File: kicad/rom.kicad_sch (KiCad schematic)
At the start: 21 parts, among them U10 2764, U11 2764, U14 X2210, U15 74LS156, U16 7400, U17 74LS244, U18 74LS244, U19 74LS245, U6 2764, U62 74LS08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

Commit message: update kicad project
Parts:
- added U77: 74LS04, Package_DIP:DIP-14_W7.62mm, symbol 74xx:74LS04
- C5, C6: seq_coord (none) -> C4
- R5, RN4: seq_coord (none) -> C3
- R63, SP0: seq_coord (none) -> C10
- SP1: seq_coord (none) -> B1
- U10: footprint seequa_footprints:DIP-40_Socket_Compact -> Package_DIP:DIP-28_W15.24mm; seq_coord (none) -> B7; seq_silkscreen (none) -> E
- U11: footprint seequa_footprints:DIP-40_Socket_Compact -> Package_DIP:DIP-28_W15.24mm; seq_coord (none) -> B8; seq_silkscreen (none) -> F
- U14: seq_coord (none) -> C1
- U15: seq_coord (none) -> C2
- U16: seq_coord (none) -> C3; seq_silkscreen (none) -> 00
- U17: seq_coord (none) -> C5
- U18: seq_coord (none) -> C6; seq_notes ROM Address Buffer 8-10 -> ROM Address Buffer 8-13
- U19: seq_coord (none) -> C7; seq_notes ROM Data Bus Transceiver -> RAM/ROM Data Bus Transceiver; seq_silkscreen (none) -> LS245
- U6: footprint seequa_footprints:DIP-40_Socket_Compact -> Package_DIP:DIP-28_W15.24mm; seq_coord (none) -> B1
- U62: seq_coord (none) -> B10; seq_silkscreen (none) -> LS08
- U7: footprint seequa_footprints:DIP-40_Socket_Compact -> Package_DIP:DIP-28_W15.24mm; seq_coord (none) -> B3
- U74: seq_coord (none) -> D11
- U8: footprint seequa_footprints:DIP-40_Socket_Compact -> Package_DIP:DIP-28_W15.24mm; seq_coord (none) -> B4; seq_silkscreen (none) -> C
- U9: footprint seequa_footprints:DIP-40_Socket_Compact -> Package_DIP:DIP-28_W15.24mm; seq_coord (none) -> B6; seq_silkscreen (none) -> D
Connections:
- net GND: now also C6.2; no longer C6.1
- net ~{MEMR}: now also U77.11
- net ~{ROM_{CE}}: now reaches U7.20 (~{CE}), U74.14 (I/~{O_{3}})
- net at RN4.6 (R5.2), U15.6 (Q1a), U16.9: now also C6.1; no longer C6.2
- net ~{ARRAY_RECALL}: now reaches U14.10 (~{ARRAY_RECALL}), U16.11
- net DATA_DIR: now reaches U19.1 (A->B)
- net MRDC renamed MEMR
- net MEMR: now also U77.10
- net NVR_NAND_EXT renamed ~{RESET_{BRD}}
- net PALETTE0_SEL renamed ~{PALETTE0_{WR}}
- net PALETTE1_SEL renamed ~{PALETTE1_{WR}}
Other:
- note added: "To RAM (Page 3)"
- moved on the sheet: C6, U10, U11, U18, U6, U9

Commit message: More updates
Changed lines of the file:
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@@
+		)
+	)
+	(label "D[0..7]"
+		(at 337.82 139.7 270)
+		(effects
+			(font
+				(size 1.27 1.27)
+			)
+			(justify right bottom)
 		)
 	)

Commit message: Updates, chameleon logo
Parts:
- RN4: value 4.7K -> 4.7KΩ
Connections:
- net ~{ROM_{CE}} is gone; now on net BANK_EN_{B}: U7.20 (~{CE}), U74.14 (I/~{O_{3}})
- net BANK_EN_{B}: no longer U74.15 (I/~{O_{4}}), U8.20 (~{CE})
- net BANK_EN_{C}: now also U74.15 (I/~{O_{4}}), U8.20 (~{CE}); no longer U74.16 (I/~{O_{5}}), U9.20 (~{CE})
- net BANK_EN_{D}: now also U74.16 (I/~{O_{5}}), U9.20 (~{CE}); no longer U10.20 (~{CE}), U74.17 (I/~{O_{6}})
- net BANK_EN_{E}: now also U10.20 (~{CE}), U74.17 (I/~{O_{6}}); no longer U11.20 (~{CE}), U74.18 (I/~{O_{7}})
- new net BANK_EN_{F}: U11.20 (~{CE}), U74.18 (I/~{O_{7}})
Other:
- moved on the sheet: U62E

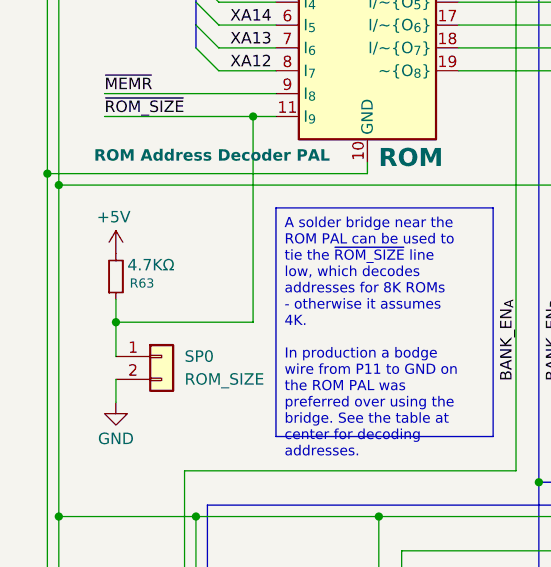
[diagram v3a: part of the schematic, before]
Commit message: A little work on composite output and GPIB
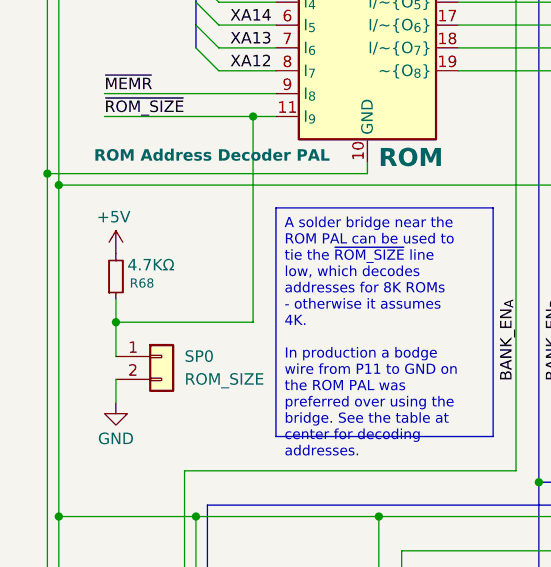
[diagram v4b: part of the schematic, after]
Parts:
- renumbered R63 to R68
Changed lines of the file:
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@@
 			(table_cell "~{ROM_SIZE}"
 				(exclude_from_sim no)
-				(at 240.03 226.06 0)
+				(at 158.75 226.06 0)
 				(size 15.24 2.54)
 				(margins 0.9525 0.9525 0.9525 0.9525)
@@
 			(table_cell ""
 				(exclude_from_sim no)
-				(at 247.65 226.06 0)
+				(at 166.37 226.06 0)
 				(size 7.62 2.54)
 				(margins 0.9525 0.9525 0.9525 0.9525)
@@
 			(table_cell "0 (8K)"
 				(exclude_from_sim no)
-				(at 240.03 228.6 0)
+				(at 158.75 228.6 0)
 				(size 7.62 2.54)
 				(margins 0.9525 0.9525 0.9525 0.9525)
@@
 			(table_cell "1 (4K)"
 				(exclude_from_sim no)
-				(at 247.65 228.6 0)
+				(at 166.37 228.6 0)
 				(size 7.62 2.54)
 				(margins 0.9525 0.9525 0.9525 0.9525)
@@
 				)
 			)
-			(table_cell "FE000"
+			(table_cell "FA000"
 				(exclude_from_sim no)
-				(at 240.03 231.14 0)
+				(at 158.75 231.14 0)
 				(size 7.62 2.54)
 				(margins 0.9525 0.9525 0.9525 0.9525)
@@
 				)
 			)
-			(table_cell "FF000"
+			(table_cell "FD000"
 				(exclude_from_sim no)
-				(at 247.65 231.14 0)
+				(at 166.37 231.14 0)
 				(size 7.62 2.54)
 				(margins 0.9525 0.9525 0.9525 0.9525)
@@
 			(table_cell "~{ROM_SIZE}"
 				(exclude_from_sim no)
-				(at 35.56 226.06 0)
+				(at 240.03 226.06 0)
 				(size 15.24 2.54)
 				(margins 0.9525 0.9525 0.9525 0.9525)
@@
 			(table_cell ""
 				(exclude_from_sim no)
-				(at 43.18 226.06 0)
+				(at 247.65 226.06 0)
 				(size 7.62 2.54)
 				(margins 0.9525 0.9525 0.9525 0.9525)
@@
 			(table_cell "0 (8K)"
 				(exclude_from_sim no)
-				(at 35.56 228.6 0)
+				(at 240.03 228.6 0)
 				(size 7.62 2.54)
 				(margins 0.9525 0.9525 0.9525 0.9525)
@@
 			(table_cell "1 (4K)"
 				(exclude_from_sim no)
-				(at 43.18 228.6 0)
+				(at 247.65 228.6 0)
 				(size 7.62 2.54)
 				(margins 0.9525 0.9525 0.9525 0.9525)
@@
 				)
 			)
-			(table_cell "F4000"
+			(table_cell "FE000"
 				(exclude_from_sim no)
-				(at 35.56 231.14 0)
+				(at 240.03 231.14 0)
 				(size 7.62 2.54)
 				(margins 0.9525 0.9525 0.9525 0.9525)
@@
 				)
 			)
-			(table_cell "FA000"
+			(table_cell "FF000"
 				(exclude_from_sim no)
-				(at 43.18 231.14 0)
+				(at 247.65 231.14 0)
 				(size 7.62 2.54)
 				(margins 0.9525 0.9525 0.9525 0.9525)
@@
 				(effects
 					(font
+						(face "Arial")
 						(size 1.27 1.27)
 					)
@@
 			(table_cell "~{ROM_SIZE}"
 				(exclude_from_sim no)
-				(at 158.75 226.06 0)
+				(at 77.47 226.06 0)
 				(size 15.24 2.54)
 				(margins 0.9525 0.9525 0.9525 0.9525)
@@
 			(table_cell ""
 				(exclude_from_sim no)
-				(at 166.37 226.06 0)
+				(at 85.09 226.06 0)
 				(size 7.62 2.54)
 				(margins 0.9525 0.9525 0.9525 0.9525)
@@
 			(table_cell "0 (8K)"
 				(exclude_from_sim no)
-				(at 158.75 228.6 0)
+				(at 77.47 228.6 0)
 				(size 7.62 2.54)
 				(margins 0.9525 0.9525 0.9525 0.9525)
@@
 			(table_cell "1 (4K)"
 				(exclude_from_sim no)
-				(at 166.37 228.6 0)
+				(at 85.09 228.6 0)
 				(size 7.62 2.54)
 				(margins 0.9525 0.9525 0.9525 0.9525)
@@
 				)
 			)
-			(table_cell "FA000"
+			(table_cell "F6000"
 				(exclude_from_sim no)
-				(at 158.75 231.14 0)
+				(at 77.47 231.14 0)
 				(size 7.62 2.54)
 				(margins 0.9525 0.9525 0.9525 0.9525)
@@
 				)
 			)
-			(table_cell "FD000"
+			(table_cell "FB000"
 				(exclude_from_sim no)
-				(at 166.37 231.14 0)
+				(at 85.09 231.14 0)
 				(size 7.62 2.54)
 				(margins 0.9525 0.9525 0.9525 0.9525)
@@
 				(effects
 					(font
-						(face "Arial")
 						(size 1.27 1.27)
 					)
@@
 			(table_cell "~{ROM_SIZE}"
 				(exclude_from_sim no)
-				(at 77.47 226.06 0)
+				(at 35.56 226.06 0)
 				(size 15.24 2.54)
 				(margins 0.9525 0.9525 0.9525 0.9525)
@@
 			(table_cell ""
 				(exclude_from_sim no)
-				(at 85.09 226.06 0)
+				(at 43.18 226.06 0)
 				(size 7.62 2.54)
 				(margins 0.9525 0.9525 0.9525 0.9525)
@@
 			(table_cell "0 (8K)"
 				(exclude_from_sim no)
-				(at 77.47 228.6 0)
+				(at 35.56 228.6 0)
 				(size 7.62 2.54)
 				(margins 0.9525 0.9525 0.9525 0.9525)
@@
 			(table_cell "1 (4K)"
 				(exclude_from_sim no)
-				(at 85.09 228.6 0)
+				(at 43.18 228.6 0)
 				(size 7.62 2.54)
 				(margins 0.9525 0.9525 0.9525 0.9525)
@@
 				)
 			)
-			(table_cell "F6000"
+			(table_cell "F4000"
 				(exclude_from_sim no)
-				(at 77.47 231.14 0)
+				(at 35.56 231.14 0)
 				(size 7.62 2.54)
 				(margins 0.9525 0.9525 0.9525 0.9525)
@@
 				)
 			)
-			(table_cell "FB000"
+			(table_cell "FA000"
 				(exclude_from_sim no)
-				(at 85.09 231.14 0)
+				(at 43.18 231.14 0)
 				(size 7.62 2.54)
 				(margins 0.9525 0.9525 0.9525 0.9525)
@@
 		)
 		(instances
-			(project ""
+			(project "seequa_chameleon"
 				(path "/ae890d4c-6a02-4621-80ce-7ef4317218ea/1f479d5d-523c-4c68-a2ad-89d48e5c8823"
 					(reference "U74")
@@
 		)
 		(instances
-			(project ""
+			(project "seequa_chameleon"
 				(path "/ae890d4c-6a02-4621-80ce-7ef4317218ea/1f479d5d-523c-4c68-a2ad-89d48e5c8823"
 					(reference "#PWR04")
@@
 		(on_board yes)
 		(dnp no)
-		(property "Reference" "R63"
+		(property "Reference" "R68"
 			(at 24.384 134.112 0)
 			(effects
@@
 			(project "seequa_chameleon"
 				(path "/ae890d4c-6a02-4621-80ce-7ef4317218ea/1f479d5d-523c-4c68-a2ad-89d48e5c8823"
-					(reference "R63")
+					(reference "R68")
 					(unit 1)
 				)
@@
 		)
 		(instances
-			(project ""
+			(project "seequa_chameleon"
 				(path "/ae890d4c-6a02-4621-80ce-7ef4317218ea/1f479d5d-523c-4c68-a2ad-89d48e5c8823"
 					(reference "U6")
@@
 		)
 		(instances
-			(project ""
+			(project "seequa_chameleon"
 				(path "/ae890d4c-6a02-4621-80ce-7ef4317218ea/1f479d5d-523c-4c68-a2ad-89d48e5c8823"
 					(reference "#PWR02")
@@
 		)
 		(instances
-			(project ""
+			(project "seequa_chameleon"
 				(path "/ae890d4c-6a02-4621-80ce-7ef4317218ea/1f479d5d-523c-4c68-a2ad-89d48e5c8823"
 					(reference "SP0")
@@
 		)
 		(instances
-			(project ""
+			(project "seequa_chameleon"
 				(path "/ae890d4c-6a02-4621-80ce-7ef4317218ea/1f479d5d-523c-4c68-a2ad-89d48e5c8823"
 					(reference "#PWR058")
@@
 		)
 		(instances
-			(project ""
+			(project "seequa_chameleon"
 				(path "/ae890d4c-6a02-4621-80ce-7ef4317218ea/1f479d5d-523c-4c68-a2ad-89d48e5c8823"
 					(reference "U62")
